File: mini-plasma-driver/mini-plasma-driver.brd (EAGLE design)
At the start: 102.3 x 82.3 mm, 93 parts, among them IC1 IR21844D, IC2 74LS19N, IC3 NE555N, IC5 IR21844D, J1 12v IN, Q1 STH60N10W, Q3 2N2369, Q4 2N2369, Q7 STH60N10W, Q8 STH60N10W, Q9 STH60N10W

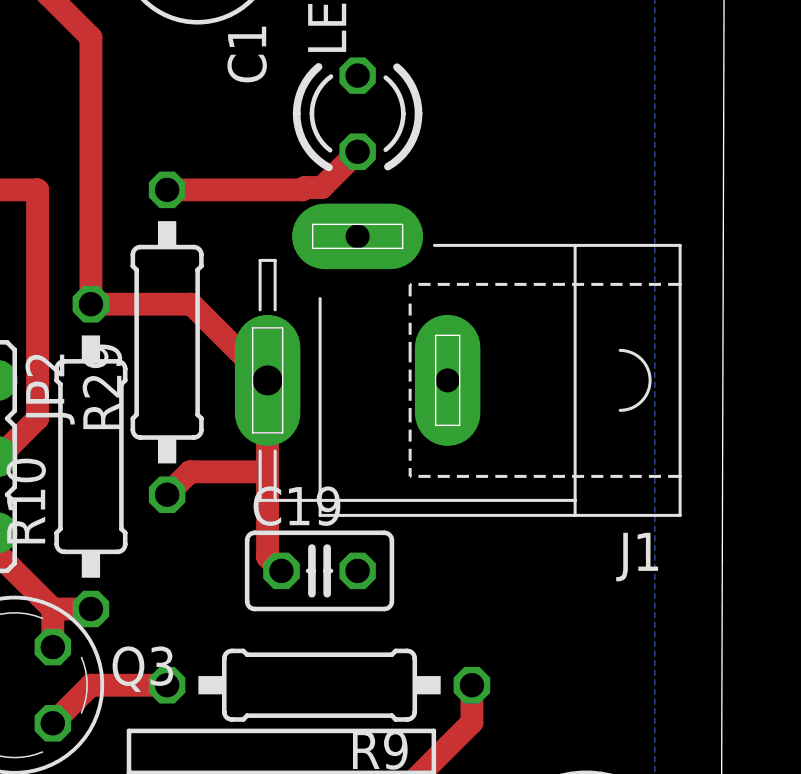
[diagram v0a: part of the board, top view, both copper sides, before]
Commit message: replace 12v barrel connector
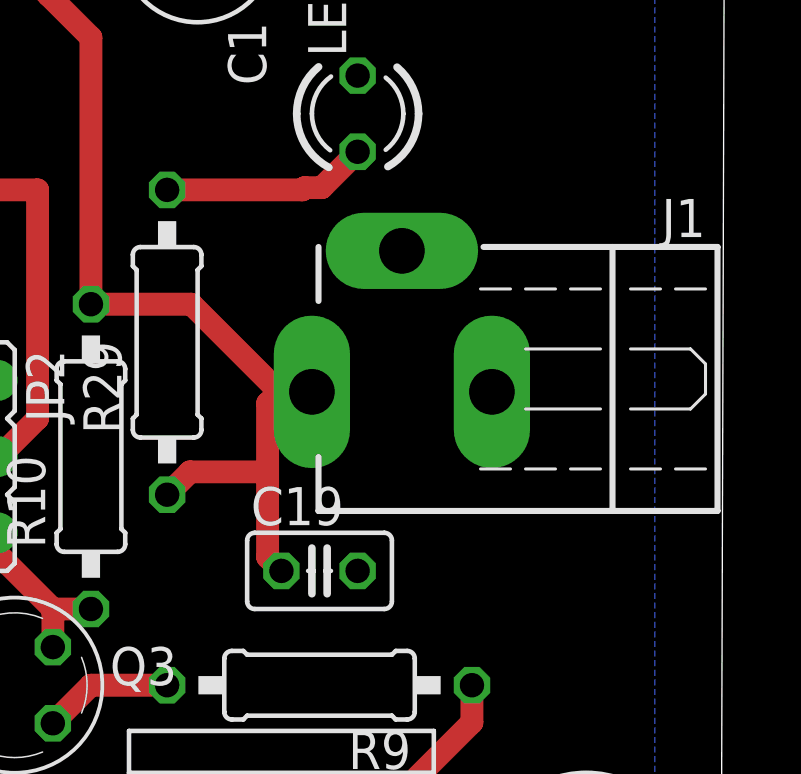
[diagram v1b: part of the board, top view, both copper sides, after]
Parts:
- J1: value 12v IN -> DC21P; device con-jack:SPC4077 -> keves:CUI-PJ-102AH
- moved J1 4.58 mm to (87.4, 23.4), turned to 270 degrees
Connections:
- net 12V: now also J1.+; no longer J1.3
- net GND: now also J1.-; no longer J1.1
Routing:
- net 12V: track 190.9 -> 192.3 mm
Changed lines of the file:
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@@
 <element name="IC3" library="linear" library_urn="urn:adsk.eagle:library:262" package="DIL08" package3d_urn="urn:adsk.eagle:package:16409/2" value="NE555N" x="62.23" y="8.89"/>
 <element name="IC5" library="irs" package="DIL14" value="IR21844D" x="50.292" y="44.704"/>
-<element name="J1" library="con-jack" library_urn="urn:adsk.eagle:library:154" package="SPC4077" package3d_urn="urn:adsk.eagle:package:7492/1" value="12v IN" x="88.9" y="19.05" rot="R180">
-<attribute name="MF" value="" x="88.9" y="19.05" size="1.778" layer="27" rot="R180" display="off"/>
-<attribute name="MPN" value="" x="88.9" y="19.05" size="1.778" layer="27" rot="R180" display="off"/>
-<attribute name="OC_FARNELL" value="unknown" x="88.9" y="19.05" size="1.778" layer="27" rot="R180" display="off"/>
-<attribute name="OC_NEWARK" value="unknown" x="88.9" y="19.05" size="1.778" layer="27" rot="R180" display="off"/>
-</element>
 <element name="JP1" library="jumper" library_urn="urn:adsk.eagle:library:252" package="JP1" package3d_urn="urn:adsk.eagle:package:15455/1" value="" x="9.144" y="65.786" rot="MR180"/>
 <element name="JP2" library="jumper" library_urn="urn:adsk.eagle:library:252" package="JP2" package3d_urn="urn:adsk.eagle:package:15452/1" value="" x="76.2" y="16.51" rot="R270"/>
@@
 <attribute name="BOM" value="EXCLUDE" x="17" y="77" size="1.778" layer="27" display="off"/>
 </element>
+<element name="J1" library="keves" package="CUI-PJ-102AH" value="DC21P" x="87.376" y="23.368" rot="R270"/>
 </elements>
 <signals>
@@
 <contactref element="R29" pad="1"/>
 <contactref element="C19" pad="1"/>
-<contactref element="J1" pad="3"/>
 <contactref element="JP3" pad="1"/>
 <wire x1="86.36" y1="12.7" x2="85.9" y2="13.16" width="0.762" layer="1"/>
 <wire x1="85.9" y1="13.16" x2="85.9" y2="16.002" width="0.762" layer="1"/>
-<wire x1="85.9" y1="16.002" x2="85.9" y2="19.05" width="0.762" layer="1"/>
 <wire x1="82.55" y1="15.24" x2="83.312" y2="16.002" width="0.762" layer="1"/>
 <wire x1="83.312" y1="16.002" x2="85.9" y2="16.002" width="0.762" layer="1"/>
 <wire x1="80.01" y1="21.59" x2="83.36" y2="21.59" width="0.762" layer="1"/>
-<wire x1="83.36" y1="21.59" x2="85.9" y2="19.05" width="0.762" layer="1"/>
 <wire x1="69.85" y1="5.08" x2="66.04" y2="5.08" width="0.762" layer="1"/>
 <wire x1="58.42" y1="12.7" x2="60.706" y2="10.414" width="0.762" layer="1"/>
@@
 <wire x1="83.566" y1="34.544" x2="83.566" y2="37.592" width="0.762" layer="1"/>
 <wire x1="83.566" y1="37.592" x2="83.566" y2="40.894" width="0.762" layer="1"/>
+<contactref element="J1" pad="+"/>
+<wire x1="83.36" y1="21.59" x2="86.282" y2="18.668" width="0.762" layer="1"/>
+<wire x1="86.282" y1="18.668" x2="87.376" y2="18.668" width="0.762" layer="1"/>
+<wire x1="85.9" y1="16.002" x2="85.9" y2="18.286" width="0.762" layer="1"/>
+<wire x1="85.9" y1="18.286" x2="86.282" y2="18.668" width="0.762" layer="1"/>
 </signal>
 <signal name="GND">
@@
 <contactref element="IC2" pad="5"/>
 <contactref element="C19" pad="2"/>
-<contactref element="J1" pad="1"/>
 <contactref element="JP3" pad="2"/>
 <contactref element="LED3_GREEN" pad="K"/>
@@
 <vertex x="98.552" y="2.032"/>
 </polygon>
+<contactref element="J1" pad="-"/>
 </signal>
 <signal name="N$1">
